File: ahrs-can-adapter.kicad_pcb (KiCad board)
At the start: 2 copper layers, 61.3 x 77 mm, 44 parts, among them J1 Flight Power, J2 Flight Telem, J3 CAN IN, J4 CAN OUT, SW1 Reset, U1 MPM3610-adafruit, U2 uA7805, U3 LTC2875-S8, U4 STM32F107R_B-C_Tx, U5 VCAN26A2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

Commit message: Fixed crystal circuit
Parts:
- U1: value MPM3610-adafruit -> MPM3610-adafruit 5V
- U2: value uA7805 -> UA78M33CDCYR
- U4: value STM32F107R_B-C_Tx -> STM32F107RCT6
- moved C5 3.09 mm to (161.9, 98.5)
- moved Y1 2.66 mm to (162.0, 101.8)
- moved C6 2.30 mm to (162.1, 105.2)
- turned C4 to 180 degrees
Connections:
- C5 pad 1: Net-(C5-Pad1) -> Net-(U4-PD1)
- C6 pad 1: Net-(C6-Pad1) -> Net-(U4-PD0)
- Y1 pad 2: Net-(C6-Pad1) -> unconnected-(Y1-Pad2)
- Y1 pad 4: Net-(C5-Pad1) -> unconnected-(Y1-Pad4)
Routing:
- net GND: track 117.0 -> 137.6 mm, vias 43 -> 52
- net CANL1: track 39.7 -> 50.2 mm, vias 2 -> 0
- net CANL2: track 41.8 -> 49.0 mm
- net Net-(U4-PD0): track 6.47 -> 12.6 mm
- net Net-(C6-Pad1): track 5.90 -> 0.00 mm
- net Net-(U4-PD1): track 3.85 -> 9.42 mm
- net CANH1: track 64.5 -> 59.0 mm, vias 2 -> 1
- net +5V: track 40.8 -> 35.7 mm
- net NRST: track 68.4 -> 73.2 mm, vias 4 -> 2
- net TX: track 16.5 -> 20.6 mm, vias 0 -> 2
- net Current: track 50.3 -> 53.3 mm, vias 2 -> 4
- net Net-(C5-Pad1): track 2.25 -> 0.00 mm
- net SWDIO: track 29.6 -> 31.3 mm
- net Net-(U3-TXD): track 10.4 -> 11.9 mm
- net Net-(U3-RXD): track 15.8 -> 16.4 mm
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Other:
- rule pad_to_mask_clearance: 0 -> 0.0508

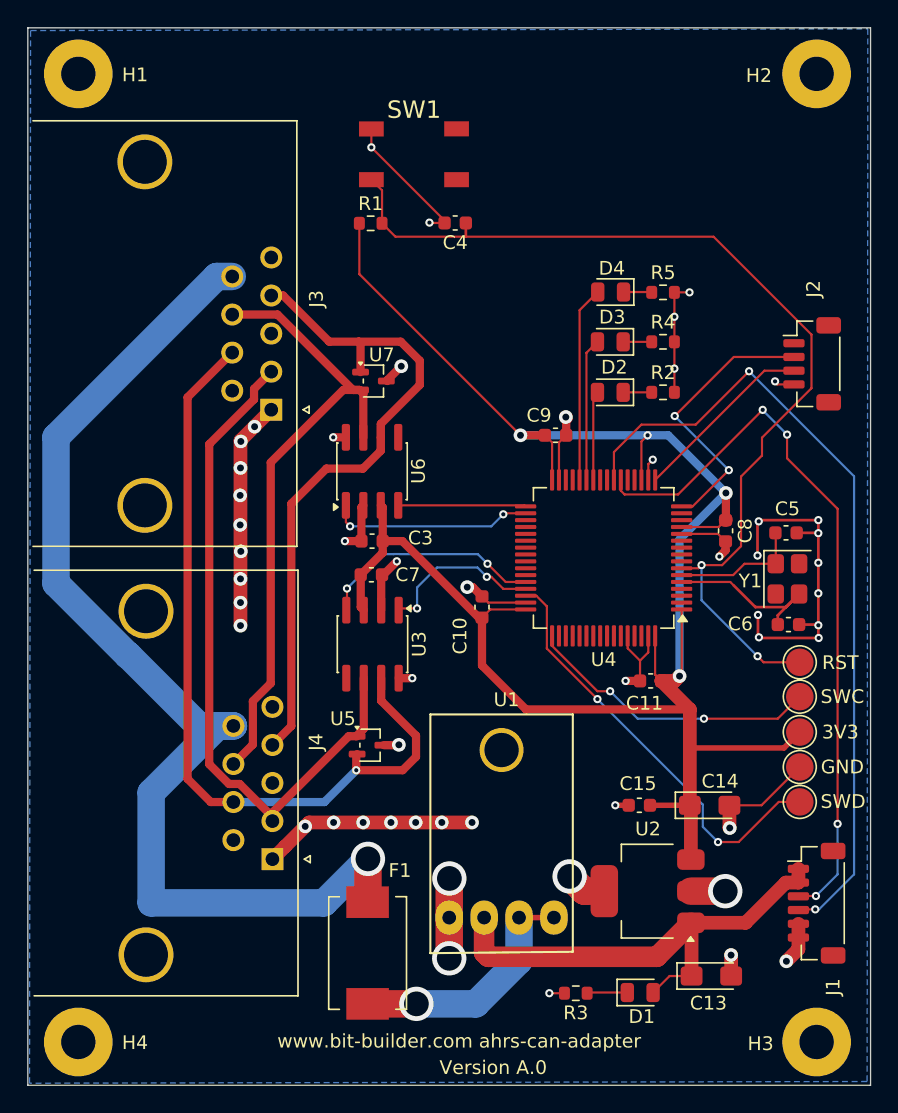
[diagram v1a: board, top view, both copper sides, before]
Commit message: Changed flight board connectors
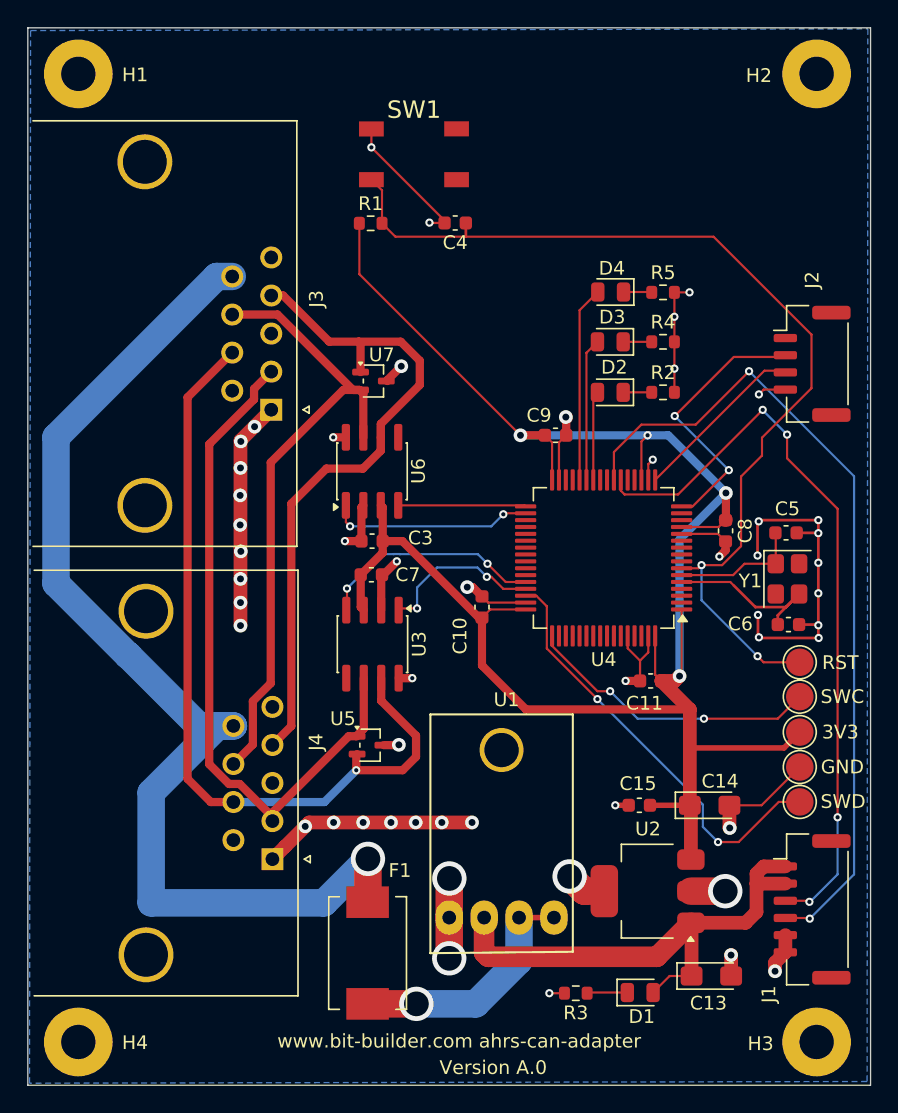
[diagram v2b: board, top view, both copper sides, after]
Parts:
- J1: footprint Connector_JST:JST_SH_BM06B-SRSS-TB_1x06-1MP_P1.00mm_Vertical -> Connector_JST:JST_GH_BM06B-GHS-TBT_1x06-1MP_P1.25mm_Vertical
- J2: footprint Connector_JST:JST_SH_BM04B-SRSS-TB_1x04-1MP_P1.00mm_Vertical -> Connector_JST:JST_GH_BM04B-GHS-TBT_1x04-1MP_P1.25mm_Vertical
- moved J1 0.56 mm to (163.8, 125.9)
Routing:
- net +5V: track 35.7 -> 37.9 mm
- net Voltage: track 59.1 -> 60.4 mm
- net Current: track 53.3 -> 54.5 mm

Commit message: Changed MCU to stm32g474ret6
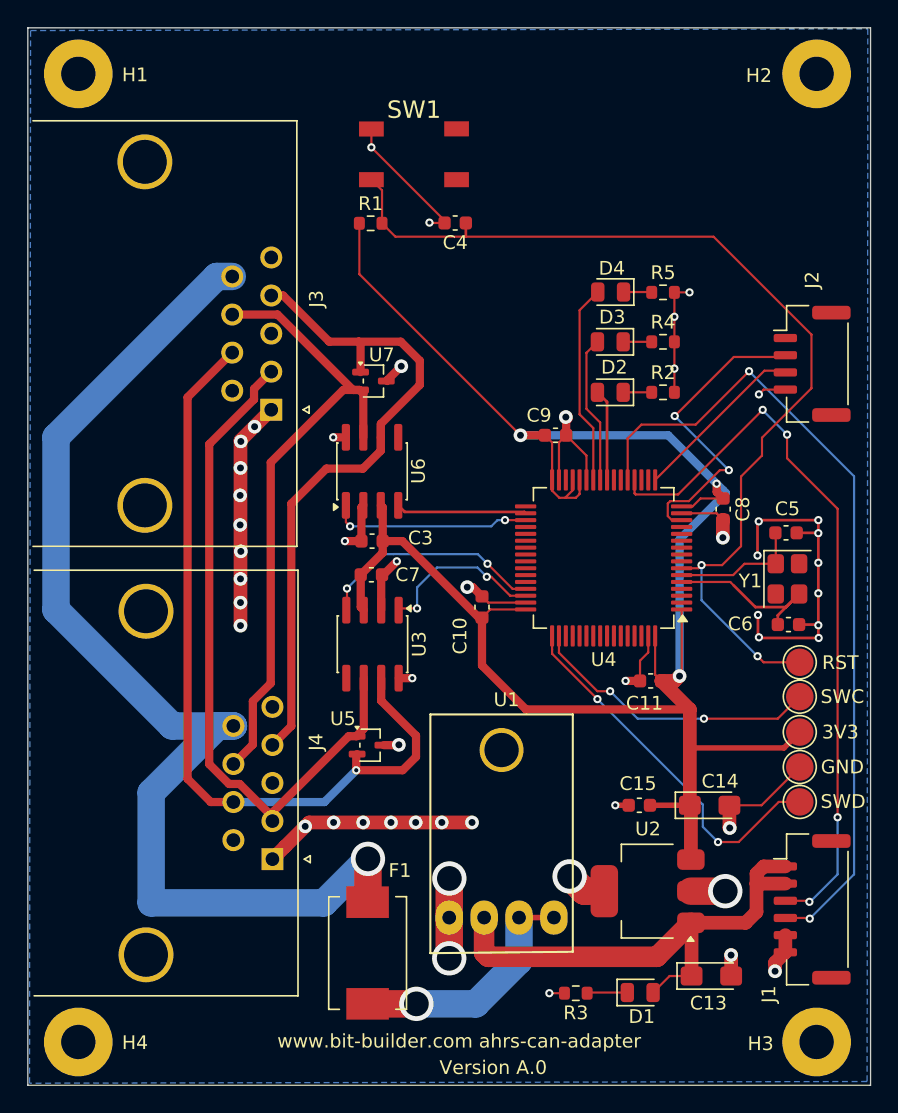
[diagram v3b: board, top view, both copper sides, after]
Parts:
- U4: value STM32F107RCT6 -> STM32G474RETx
- moved C8 1.58 mm to (157.3, 96.8)
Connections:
- U4 pad 12: GND -> unconnected-(U4-PA0-Pad12)
- U4 pad 13: +3.3V -> unconnected-(U4-PA1-Pad13)
- U4 pad 14: unconnected-(U4-PA0-Pad14) -> TX
- U4 pad 15: unconnected-(U4-PA1-Pad15) -> GND
- U4 pad 16: TX -> +3.3V
- U4 pad 18: GND -> unconnected-(U4-PA4-Pad18)
- U4 pad 19: +3.3V -> unconnected-(U4-PA5-Pad19)
- U4 pad 20: unconnected-(U4-PA4-Pad20) -> Current
- U4 pad 21: unconnected-(U4-PA5-Pad21) -> Voltage
- U4 pad 22: Current -> unconnected-(U4-PC4-Pad22)
- U4 pad 23: Voltage -> unconnected-(U4-PC5-Pad23)
- U4 pad 24: unconnected-(U4-PC4-Pad24) -> LED1
- U4 pad 25: unconnected-(U4-PC5-Pad25) -> LED2
- U4 pad 26: LED1 -> LED3
- U4 pad 27: LED2 -> GND
- U4 pad 28: LED3 -> +3.3V
- U4 pad 29: unconnected-(U4-PB10-Pad29) -> +3.3V
- U4 pad 33: Net-(U4-PB12) -> unconnected-(U4-PB11-Pad33)
- U4 pad 34: Net-(U4-PB13) -> Net-(U4-PB12)
- U4 pad 35: unconnected-(U4-PB14-Pad35) -> Net-(U4-PB13)
- U4 pad 44: Net-(U3-RXD) -> unconnected-(U4-PA10-Pad44)
- U4 pad 45: Net-(U3-TXD) -> Net-(U3-RXD)
- U4 pad 46: SWDIO -> Net-(U3-TXD)
- U4 pad 49: SWCLK -> SWDIO
- U4 pad 50: unconnected-(U4-PA15-Pad50) -> SWCLK
- U4 pad 60: GND -> unconnected-(U4-PB7-Pad60)
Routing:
- net SWDIO: track 31.3 -> 27.2 mm
- net TX: track 20.6 -> 23.5 mm
- net +3.3V: track 142.1 -> 143.5 mm, vias 4 -> 3
- net +12V: track 81.8 -> 82.9 mm
- net Current: track 54.5 -> 53.6 mm
- net LED1: track 6.08 -> 6.66 mm
- net GND: track 137.8 -> 137.7 mm, vias 52 -> 51

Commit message: updated crystal circuit
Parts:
- added C1: 4.7uF, Capacitor_SMD:C_0603_1608Metric, F.Cu at (156.6, 109.2)
- added C12: 1uF, Capacitor_SMD:C_0603_1608Metric, F.Cu at (144.9, 85.5)
- added C16: 1uF, Capacitor_SMD:C_0603_1608Metric, F.Cu at (144.9, 88.0)
- added C2: 10nF, Capacitor_SMD:C_0603_1608Metric, F.Cu at (144.9, 83.0)
- C5, C6: value 22pF -> 6.8pF
- U4: value STM32G474RETx -> STM32G474RET6
- Y1: value 8MHz -> 24MHz; footprint Crystal:Crystal_SMD_TXC_7M-4Pin_3.2x2.5mm -> Crystal:Crystal_SMD_2016-4Pin_2.0x1.6mm
- moved C9 0.89 mm to (144.3, 91.3)
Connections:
- Y1 pad 2: unconnected-(Y1-Pad2) -> GND
- Y1 pad 4: unconnected-(Y1-Pad4) -> GND
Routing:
- net GND: track 137.7 -> 155.6 mm, vias 51 -> 55
- net +3.3V: track 143.5 -> 159.6 mm
- net +12V: track 82.9 -> 81.5 mm
- net TX: track 23.5 -> 22.4 mm, vias 2 -> 0
- net Net-(U4-PF0): track 12.6 -> 11.5 mm
- net Net-(U4-PF1): track 9.42 -> 10.1 mm
